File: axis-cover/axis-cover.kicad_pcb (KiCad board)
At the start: 2 copper layers, 66 x 18 mm, 7 parts

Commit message: Update
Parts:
- H2, H3: footprint V2_Mechanical:Mounting_Hole_2mm_Pad_5.2mm -> V2_Mechanical:MountingHole_2mm_Pad_5.2mm
- moved H1 0.25 mm to (154.5, 101.2)
- moved H2 0.25 mm to (169.0, 106.2)
- moved H3 0.25 mm to (131.0, 106.2)
- moved ICON1 0.25 mm to (123.2, 106.2)
- moved ICON2 0.25 mm to (177.0, 106.5)
- moved INFO1 0.25 mm to (150.0, 111.5)
- moved SWT1 0.25 mm to (158.0, 106.2)
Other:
- board size 66 x 18 mm -> 66 x 17.3 mm

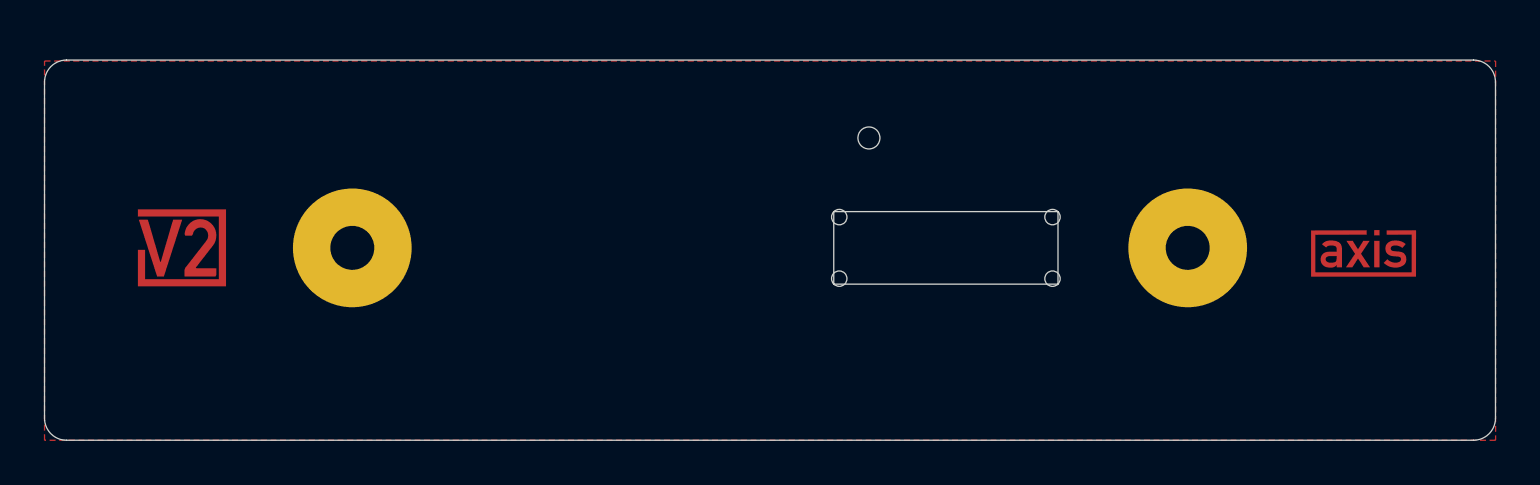
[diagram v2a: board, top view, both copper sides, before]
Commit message: Replace standoffs
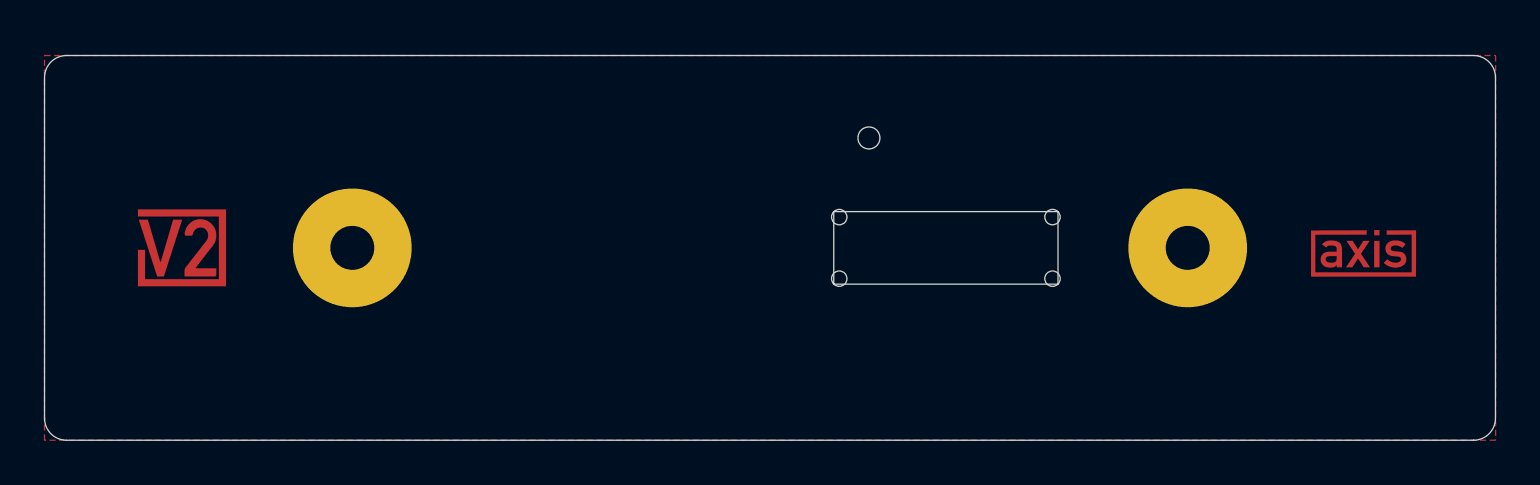
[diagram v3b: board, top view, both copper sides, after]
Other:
- board size 66 x 17.3 mm -> 66 x 17.5 mm
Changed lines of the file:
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@@
 	)
 	(gr_line
-		(start 117 98.7071)
+		(start 117 98.5)
 		(end 117 114)
 		(stroke
@@
 	)
 	(gr_line
-		(start 118 97.707107)
-		(end 182 97.707107)
+		(start 118 97.5)
+		(end 182 97.5)
 		(stroke
 			(width 0.05)
@@
 	)
 	(gr_line
-		(start 183 98.707107)
+		(start 183 98.5)
 		(end 183 114)
 		(stroke
@@
 	)
 	(gr_arc
-		(start 117 98.707107)
-		(mid 117.292893 98)
-		(end 118 97.707107)
+		(start 117 98.5)
+		(mid 117.292891 97.792889)
+		(end 118 97.5)
 		(stroke
 			(width 0.05)
@@
 	)
 	(gr_arc
-		(start 182 97.707107)
-		(mid 182.707107 98)
-		(end 183 98.707107)
+		(start 182 97.5)
+		(mid 182.707107 97.792893)
+		(end 183 98.5)
 		(stroke
 			(width 0.05)
@@
 		(polygon
 			(pts
-				(xy 183.005454 115) (xy 117 115) (xy 117 97.75) (xy 183.005454 97.75)
+				(xy 183.005454 115) (xy 117 115) (xy 117 97.5) (xy 183.005454 97.5)
 			)
 		)
